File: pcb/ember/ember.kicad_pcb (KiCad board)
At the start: 2 copper layers, 139 x 108 mm, 101 parts, among them IC1 CD4051BM96, IC2 CD4051BM96, IC3 CD4051BM96, IC4 CD4051BM96, J2 USB_C_Receptacle_USB2.0, SW1 RESET, SW2 BOOT, U1 Hall_Sensor, U10 Hall_Sensor, U11 Hall_Sensor, U12 Hall_Sensor, U13 Hall_Sensor, U14 Hall_Sensor, U15 Hall_Sensor, U16 Hall_Sensor, U17 Hall_Sensor, U18 Hall_Sensor, U19 Hall_Sensor, U2 Hall_Sensor, U20 Hall_Sensor, U21 Hall_Sensor, U22 Hall_Sensor, U23 Hall_Sensor, U24 Hall_Sensor, U25 Hall_Sensor, U26 Hall_Sensor, U27 Hall_Sensor, U28 Hall_Sensor, U29 Hall_Sensor, U3 Hall_Sensor, U30 Hall_Sensor, U31 Hall_Sensor, U32 Hall_Sensor, U33 AMS1117-3.3, U4 Hall_Sensor, U5 Hall_Sensor, U6 Hall_Sensor, U7 Hall_Sensor, U8 Hall_Sensor, U9 Hall_Sensor, Y1 16MHz

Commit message: :wrench: ver1.1
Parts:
- removed D1: D_TVS_Dual_AAC, Package_TO_SOT_SMD:SOT-23
- removed TP1: SWCLK, TestPoint:TestPoint_THTPad_D1.0mm_Drill0.5mm
- removed TP2: GND, TestPoint:TestPoint_THTPad_D1.0mm_Drill0.5mm
- removed TP3: SWDIO, TestPoint:TestPoint_THTPad_D1.0mm_Drill0.5mm
- removed TP4: RESET, TestPoint:TestPoint_THTPad_D1.0mm_Drill0.5mm
- added J1: Conn_01x04_Socket, Connector_PinSocket_2.54mm:PinSocket_1x04_P2.54mm_Vertical, B.Cu at (154.0, 70.3)
- added U34: SRV05-4, Package_TO_SOT_SMD:SOT-23-6, B.Cu at (144.5, 33.0)
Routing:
- net GND: track 775.0 -> 892.8 mm, vias 128 -> 178
- net +3.3V: track 777.7 -> 810.3 mm
- net SWCLK: track 13.8 -> 27.9 mm
- net SWDIO: track 19.3 -> 29.7 mm
- net +5V: track 40.2 -> 47.2 mm, vias 3 -> 4
- net NRST: track 47.9 -> 41.4 mm, vias 2 -> 1
- net SENS_C_CH0: track 54.3 -> 60.6 mm
- net SENS_C_CH1: track 71.1 -> 76.7 mm
- net SENS_A_CH3: track 73.6 -> 79.1 mm
- net SENS_C_CH3: track 34.0 -> 39.0 mm
- net SENS_B_CH0: track 72.3 -> 77.3 mm
- net MUX_A: track 75.4 -> 78.0 mm
- net MUX_B: track 73.6 -> 75.9 mm
- net SENS_D_CH2: track 20.6 -> 22.8 mm
- net MUX_C: track 74.4 -> 76.2 mm
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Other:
- board text added: "Ember ver1.1 designed by @kenyoshizoe"
- board text added: "GND"
- board text added: "NRST"
- board text added: "SWCLK"
- board text added: "SWDIO"
- board text removed: "Ember ver1 designed by @kenyoshizoe"

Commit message: :sparkles: add eeprom
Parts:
- added IC5: M24C64-RMN6TP, ember:SOIC127P600X175-8N, B.Cu at (144.5, 56.2)
- added R6: 10k, Resistor_SMD:R_0603_1608Metric, B.Cu at (150.5, 60.8)
- added R7: 10k, Resistor_SMD:R_0603_1608Metric, B.Cu at (149.0, 60.8)
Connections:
- IC1 pad 10: MUX_B -> MUX2_B
- IC1 pad 11: MUX_A -> MUX2_A
- IC1 pad 3: ADC0 -> ADC3
- IC1 pad 9: MUX_C -> MUX2_C
- IC2 pad 10: MUX_B -> MUX2_B
- IC2 pad 11: MUX_A -> MUX2_A
- IC2 pad 3: ADC1 -> ADC4
- IC2 pad 9: MUX_C -> MUX2_C
- IC3 pad 10: MUX_B -> MUX1_B
- IC3 pad 11: MUX_A -> MUX1_A
- IC3 pad 9: MUX_C -> MUX1_C
- IC4 pad 10: MUX_B -> MUX1_B
- IC4 pad 11: MUX_A -> MUX1_A
- IC4 pad 3: ADC3 -> ADC1
- IC4 pad 9: MUX_C -> MUX1_C
- MCU1 pad 10: MUX_A -> MUX1_A
- MCU1 pad 11: MUX_B -> MUX1_B
- MCU1 pad 12: MUX_C -> MUX1_C
- MCU1 pad 13: ADC3 -> ADC1
- MCU1 pad 25: ADC1 -> ADC4
- MCU1 pad 26: ADC0 -> ADC3
- MCU1 pad 27: unconnected-(MCU1-PB14-Pad27) -> MUX2_C
- MCU1 pad 28: unconnected-(MCU1-PB15-Pad28) -> MUX2_B
- MCU1 pad 29: unconnected-(MCU1-PA8-Pad29) -> MUX2_A
- MCU1 pad 38: unconnected-(MCU1-PA15-Pad38) -> SCL
- MCU1 pad 42: unconnected-(MCU1-PB6-Pad42) -> WC
- MCU1 pad 43: unconnected-(MCU1-PB7-Pad43) -> SDA
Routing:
- net MUX_A: track 78.0 -> 0.00 mm, vias 4 -> 0
- net MUX_C: track 76.2 -> 0.00 mm, vias 4 -> 0
- net MUX_B: track 75.9 -> 0.00 mm, vias 4 -> 0
- net MUX1_A: track 0.00 -> 51.5 mm, vias 0 -> 3
- net MUX1_B: track 0.00 -> 51.4 mm, vias 0 -> 3
- net MUX1_C: track 0.00 -> 51.1 mm, vias 0 -> 3
- net ADC0: track 41.7 -> 0.00 mm, vias 2 -> 0
- net MUX2_A: track 0.00 -> 38.8 mm, vias 0 -> 3
- net MUX2_B: track 0.00 -> 37.1 mm, vias 0 -> 3
- net MUX2_C: track 0.00 -> 35.5 mm, vias 0 -> 3
- net SCL: track 0.00 -> 26.0 mm, vias 0 -> 2
- net GND: track 892.8 -> 917.1 mm, vias 178 -> 174
- net SDA: track 0.00 -> 23.4 mm, vias 0 -> 2
- net ADC1: track 19.6 -> 39.1 mm, vias 0 -> 2
- net ADC4: track 0.00 -> 19.6 mm
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
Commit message: :bug: add 1.5k pullup to D+
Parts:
- added R8: 1.5k, Resistor_SMD:R_0603_1608Metric, B.Cu at (138.0, 34.5)
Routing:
- net +3.3V: track 815.9 -> 820.0 mm
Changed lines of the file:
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@@
     )
   )
+  (footprint "Resistor_SMD:R_0603_1608Metric" (layer "B.Cu")
+    (at 138 34.5 -90)
+    (descr "Resistor SMD 0603 (1608 Metric), square (rectangular) end terminal, IPC_7351 nominal, (Body size source: IPC-SM-782 page 72, https://www.pcb-3d.com/wordpress/wp-content/uploads/ipc-sm-782a_amendment_1_and_2.pdf), generated with kicad-footprint-generator")
+    (tags "resistor")
+    (property "LCSC" "C22843")
+    (property "Sheetfile" "ember.kicad_sch")
+    (property "Sheetname" "")
+    (property "ki_description" "Resistor, small symbol")
+    (property "ki_keywords" "R resistor")
+    (attr smd)
+    (fp_text reference "R8" (at 0 1.43 90) (layer "B.SilkS")
+        (effects (font (size 1 1) (thickness 0.15)) (justify mirror))
+    )
+    (fp_text value "1.5k" (at 0 -1.43 90) (layer "B.Fab")
+        (effects (font (size 1 1) (thickness 0.15)) (justify mirror))
+    )
+    (fp_text user "${REFERENCE}" (at 0 0 90) (layer "B.Fab")
+        (effects (font (size 0.4 0.4) (thickness 0.06)) (justify mirror))
+    )
+    (fp_line (start -0.237258 -0.5225) (end 0.237258 -0.5225)
+      (stroke (width 0.12) (type solid)) (layer "B.SilkS"))
+    (fp_line (start -0.237258 0.5225) (end 0.237258 0.5225)
+      (stroke (width 0.12) (type solid)) (layer "B.SilkS"))
+    (fp_line (start -1.48 -0.73) (end -1.48 0.73)
+      (stroke (width 0.05) (type solid)) (layer "B.CrtYd"))
+    (fp_line (start -1.48 0.73) (end 1.48 0.73)
+      (stroke (width 0.05) (type solid)) (layer "B.CrtYd"))
+    (fp_line (start 1.48 -0.73) (end -1.48 -0.73)
+      (stroke (width 0.05) (type solid)) (layer "B.CrtYd"))
+    (fp_line (start 1.48 0.73) (end 1.48 -0.73)
+      (stroke (width 0.05) (type solid)) (layer "B.CrtYd"))
+    (fp_line (start -0.8 -0.4125) (end -0.8 0.4125)
+      (stroke (width 0.1) (type solid)) (layer "B.Fab"))
+    (fp_line (start -0.8 0.4125) (end 0.8 0.4125)
+      (stroke (width 0.1) (type solid)) (layer "B.Fab"))
+    (fp_line (start 0.8 -0.4125) (end -0.8 -0.4125)
+      (stroke (width 0.1) (type solid)) (layer "B.Fab"))
+    (fp_line (start 0.8 0.4125) (end 0.8 -0.4125)
+      (stroke (width 0.1) (type solid)) (layer "B.Fab"))
+    (pad "1" smd roundrect (at -0.825 0 270) (size 0.8 0.95) (layers "B.Cu" "B.Paste" "B.Mask") (roundrect_rratio 0.25)
+      (net 63 "USB_D+") (pintype "passive"))
+    (pad "2" smd roundrect (at 0.825 0 270) (size 0.8 0.95) (layers "B.Cu" "B.Paste" "B.Mask") (roundrect_rratio 0.25)
+      (net 14 "+3.3V") (pintype "passive"))
+    (model "${KICAD6_3DMODEL_DIR}/Resistor_SMD.3dshapes/R_0603_1608Metric.wrl"
+      (offset (xyz 0 0 0))
+      (scale (xyz 1 1 1))
+      (rotate (xyz 0 0 0))
+    )
+  )
   (footprint "Package_TO_SOT_SMD:SOT-23" (layer "B.Cu")
     (at 154 38 90)
@@
   (via (at 136 72) (size 0.8) (drill 0.4) (layers "F.Cu" "B.Cu") (net 14))
   (via (at 61.5 77) (size 0.8) (drill 0.4) (layers "F.Cu" "B.Cu") (net 14))
+  (segment (start 138 35.325) (end 138 38.75) (width 0.25) (layer "B.Cu") (net 14))
   (segment (start 124.1375 117.25) (end 103.1375 117.25) (width 0.25) (layer "B.Cu") (net 14))
   (segment (start 77.25 98.25) (end 58.6375 98.25) (width 0.25) (layer "B.Cu") (net 14))
@@
   (segment (start 82.75 89) (end 80.5 91.25) (width 0.25) (layer "B.Cu") (net 14))
   (segment (start 68.44375 116.94375) (end 69.45 115.9375) (width 0.25) (layer "B.Cu") (net 14))
+  (segment (start 138 38.75) (end 137.5 39.25) (width 0.25) (layer "B.Cu") (net 14))
   (segment (start 98.5625 54.9375) (end 97.95 54.9375) (width 0.25) (layer "B.Cu") (net 14))
   (segment (start 87.788 104.212) (end 74.75 117.25) (width 0.25) (layer "B.Cu") (net 14))
@@
   (via (at 127.025 54) (size 0.8) (drill 0.4) (layers "F.Cu" "B.Cu") (net 63))
   (via (at 127.871232 34.871232) (size 0.8) (drill 0.4) (layers "F.Cu" "B.Cu") (net 63))
-  (segment (start 129.093199 33.225) (end 140 33.225) (width 0.2) (layer "B.Cu") (net 63))
   (segment (start 127.871232 34.871232) (end 127.871232 34.446967) (width 0.2) (layer "B.Cu") (net 63))
   (segment (start 154.75 28.17) (end 154.75 28.995) (width 0.2) (layer "B.Cu") (net 63))
+  (segment (start 129.093199 33.225) (end 138 33.225) (width 0.2) (layer "B.Cu") (net 63))
   (segment (start 153.725 29.057501) (end 153.725 31.0932) (width 0.2) (layer "B.Cu") (net 63))
   (segment (start 145.0375 34.55) (end 141.325 34.55) (width 0.2) (layer "B.Cu") (net 63))
@@
   (segment (start 154.75 28.995) (end 154.7 29.045) (width 0.2) (layer "B.Cu") (net 63))
   (segment (start 153.75 29.032501) (end 153.725 29.057501) (width 0.2) (layer "B.Cu") (net 63))
+  (segment (start 138 33.675) (end 138 33.225) (width 0.2) (layer "B.Cu") (net 63))
   (segment (start 148.295313 33.225) (end 147.570313 33.95) (width 0.2) (layer "B.Cu") (net 63))
   (segment (start 126.725001 60.312501) (end 126.725001 54.299999) (width 0.2) (layer "B.Cu") (net 63))
+  (segment (start 138 33.225) (end 140 33.225) (width 0.2) (layer "B.Cu") (net 63))
   (segment (start 141.325 34.55) (end 140 33.225) (width 0.2) (layer "B.Cu") (net 63))
   (segment (start 126.75 60.3375) (end 126.725001 60.312501) (width 0.2) (layer "B.Cu") (net 63))

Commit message: :wrench: add VTref Pin
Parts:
- removed J1: Conn_01x04_Socket, Connector_PinSocket_2.54mm:PinSocket_1x04_P2.54mm_Vertical
- added J3: Conn_01x05_Socket, Connector_PinSocket_2.54mm:PinSocket_1x05_P2.54mm_Vertical, B.Cu at (163.5, 61.4)
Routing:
- net SWDIO: track 29.7 -> 38.5 mm
- net GND: track 917.1 -> 908.9 mm
- net SWCLK: track 27.9 -> 35.8 mm
- net +3.3V: track 820.0 -> 827.1 mm, vias 34 -> 35
- net NRST: track 41.4 -> 44.0 mm, vias 1 -> 0
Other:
- board text added: "VTref"

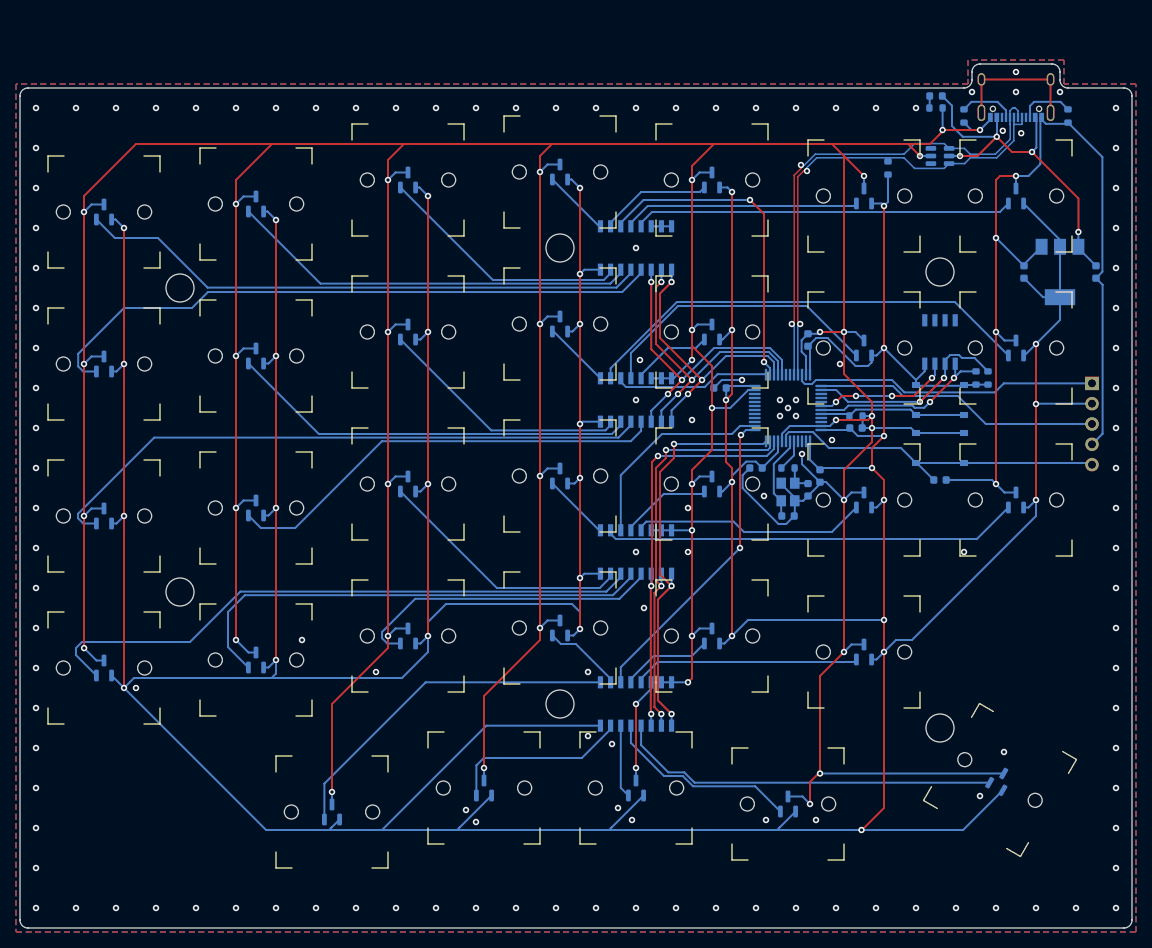
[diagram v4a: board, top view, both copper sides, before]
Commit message: change hall size 3.5mm→2.2mm(M2)
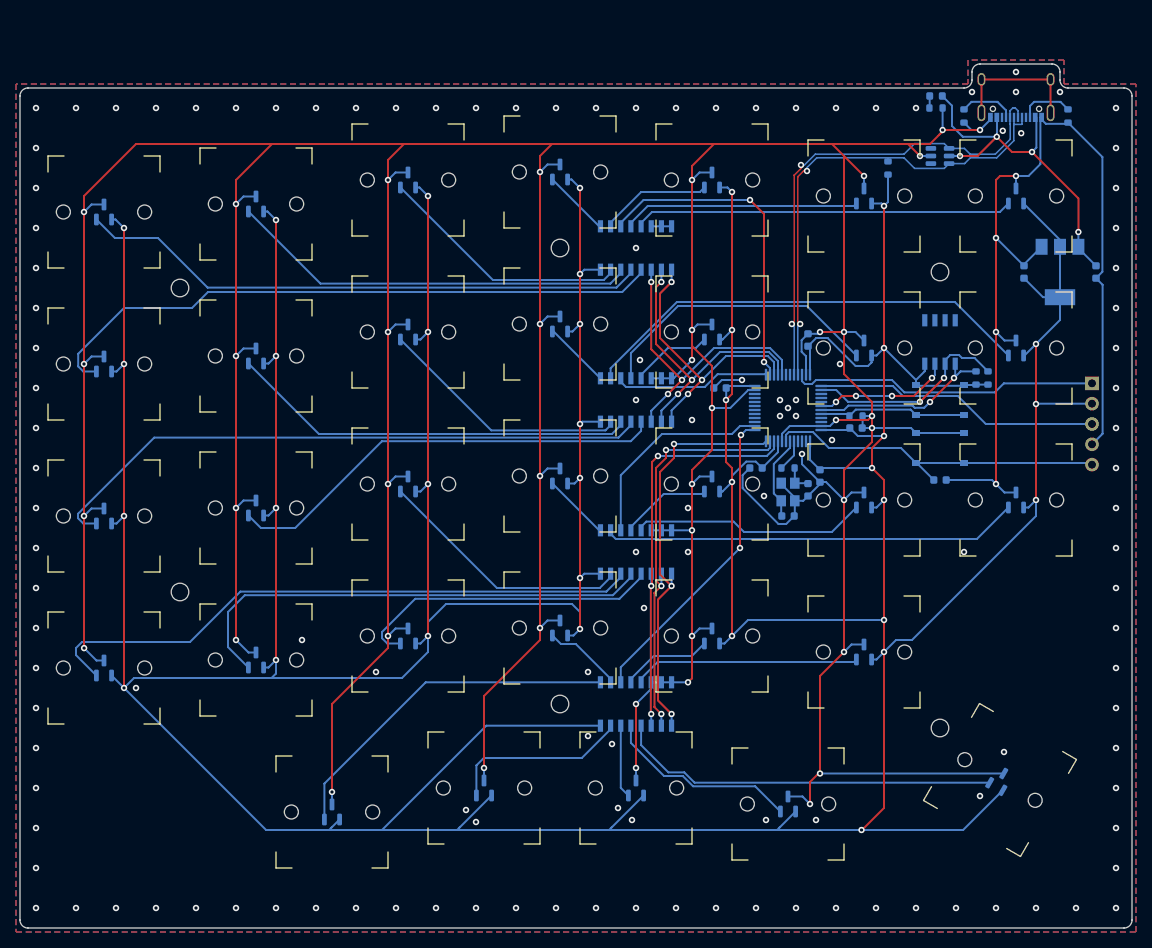
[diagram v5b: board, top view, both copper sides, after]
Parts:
- H33, H34, H35, H36, H37, H38: footprint MountingHole:MountingHole_3.5mm -> MountingHole:MountingHole_2.2mm_M2

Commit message: :sparkles: change usb connector position
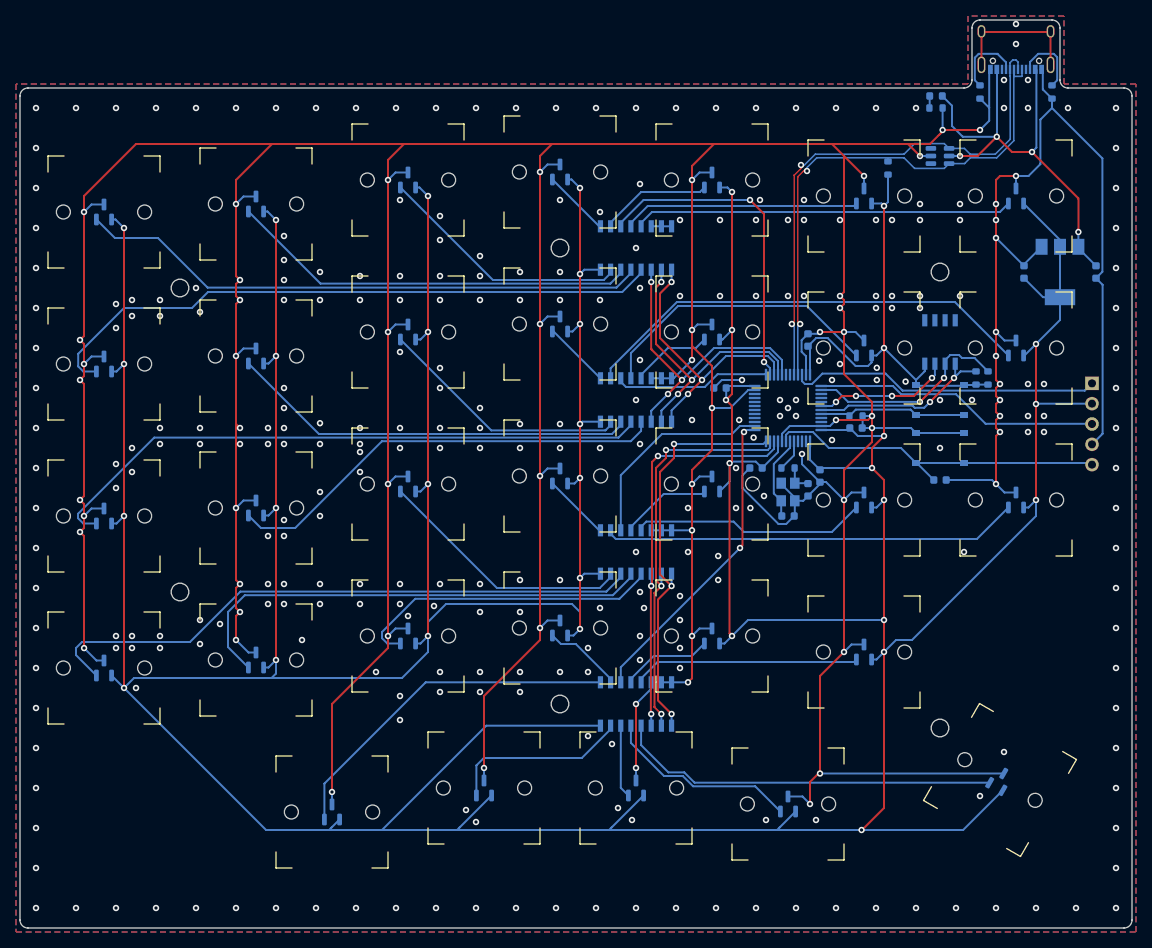
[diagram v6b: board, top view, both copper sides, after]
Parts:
- moved J2 6.00 mm to (154.0, 18.5)
- moved R1 3.61 mm to (149.5, 25.0)
- moved R2 3.61 mm to (158.5, 25.0)
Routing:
- net GND: track 908.9 -> 926.6 mm, vias 174 -> 362
- net +5V: track 47.2 -> 59.2 mm
- net USB_D+: track 60.4 -> 67.3 mm
- net USB_D-: track 61.1 -> 67.1 mm
- net Net-(J2-CC1): track 6.96 -> 9.14 mm
- net Net-(J2-CC2): track 6.78 -> 8.71 mm
- net +3.3V: track 827.1 -> 828.2 mm
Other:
- board size 139 x 108 mm -> 139 x 113.5 mm

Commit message: :sparkles: replace cd4052->ad708
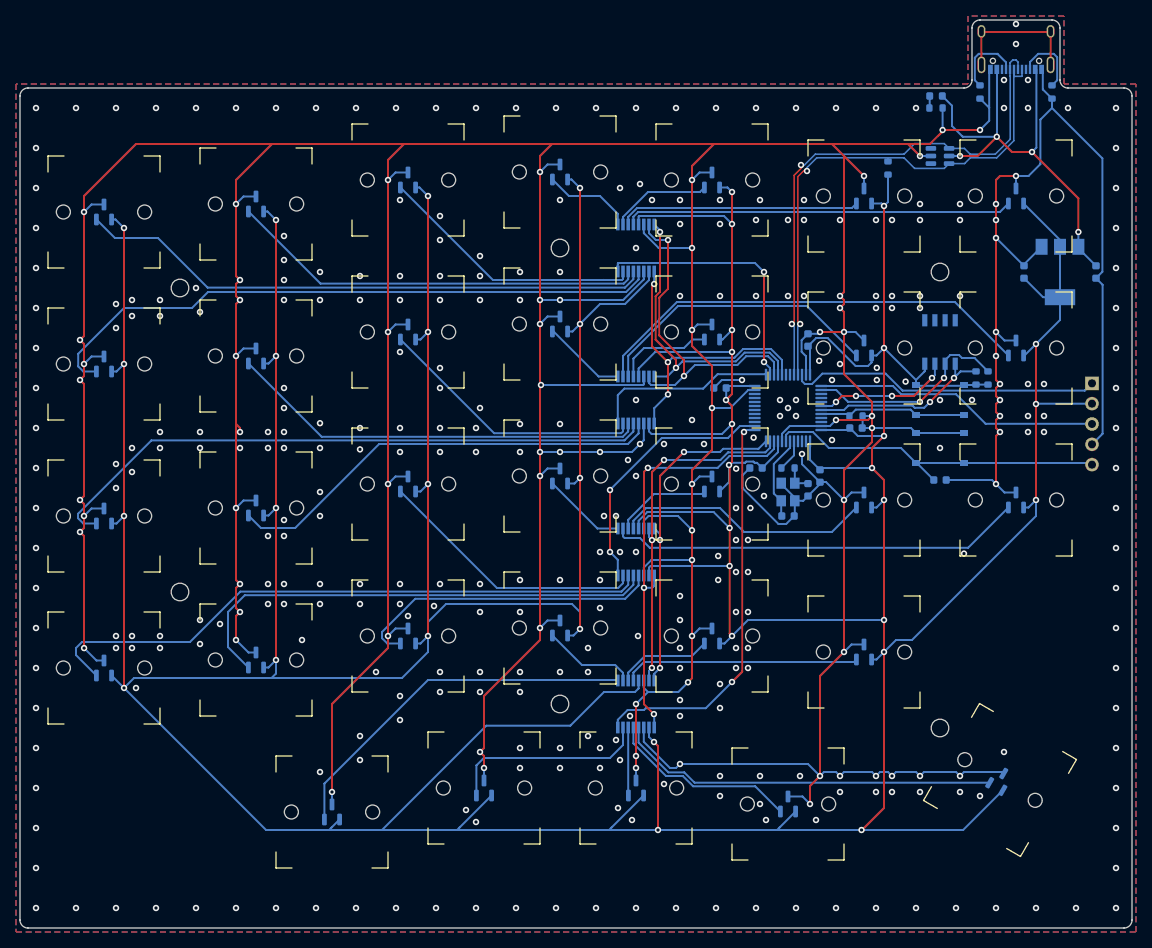
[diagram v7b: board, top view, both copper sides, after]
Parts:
- IC1, IC2, IC3, IC4: value CD4051BM96 -> ADG708BRUZ-REEL7; footprint ember:SOIC127P600X175-16N -> ember:SOP65P640X120-16N
- turned IC1 to 90 degrees
- turned IC2 to 90 degrees
- turned IC3 to 90 degrees
- turned IC4 to 90 degrees
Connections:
- IC1 pad 1: SENS_A_CH4 -> MUX2_A
- IC1 pad 10: MUX2_B -> SENS_A_CH6
- IC1 pad 11: MUX2_A -> SENS_A_CH7
- IC1 pad 12: SENS_A_CH3 -> SENS_A_CH5
- IC1 pad 13: SENS_A_CH0 -> +3.3V
- IC1 pad 14: SENS_A_CH1 -> GND
- IC1 pad 15: SENS_A_CH2 -> MUX2_C
- IC1 pad 16: +3.3V -> MUX2_B
- IC1 pad 2: SENS_A_CH6 -> +3.3V
- IC1 pad 3: ADC3 -> GND
- IC1 pad 4: SENS_A_CH7 -> SENS_A_CH3
- IC1 pad 5: SENS_A_CH5 -> SENS_A_CH0
- IC1 pad 6: GND -> SENS_A_CH1
- IC1 pad 7: GND -> SENS_A_CH2
- IC1 pad 8: GND -> ADC3
- IC1 pad 9: MUX2_C -> SENS_A_CH4
- IC2 pad 1: SENS_B_CH4 -> MUX2_A
- IC2 pad 10: MUX2_B -> SENS_B_CH6
- IC2 pad 11: MUX2_A -> SENS_B_CH7
- IC2 pad 12: SENS_B_CH3 -> SENS_B_CH5
- IC2 pad 13: SENS_B_CH0 -> +3.3V
- IC2 pad 14: SENS_B_CH1 -> GND
- IC2 pad 15: SENS_B_CH2 -> MUX2_C
- IC2 pad 16: +3.3V -> MUX2_B
- IC2 pad 2: SENS_B_CH6 -> +3.3V
- IC2 pad 3: ADC4 -> GND
- IC2 pad 4: SENS_B_CH7 -> SENS_B_CH3
- IC2 pad 5: SENS_B_CH5 -> SENS_B_CH0
- IC2 pad 6: GND -> SENS_B_CH1
- IC2 pad 7: GND -> SENS_B_CH2
- IC2 pad 8: GND -> ADC4
- IC2 pad 9: MUX2_C -> SENS_B_CH4
- IC3 pad 1: SENS_C_CH4 -> MUX1_A
- IC3 pad 10: MUX1_B -> SENS_C_CH6
- IC3 pad 11: MUX1_A -> SENS_C_CH7
- IC3 pad 12: SENS_C_CH3 -> SENS_C_CH5
- IC3 pad 13: SENS_C_CH0 -> +3.3V
- IC3 pad 14: SENS_C_CH1 -> GND
- IC3 pad 15: SENS_C_CH2 -> MUX1_B
- IC3 pad 16: +3.3V -> MUX1_C
- IC3 pad 2: SENS_C_CH6 -> +3.3V
- IC3 pad 3: ADC2 -> GND
- IC3 pad 4: SENS_C_CH7 -> SENS_C_CH3
- IC3 pad 5: SENS_C_CH5 -> SENS_C_CH0
- IC3 pad 6: GND -> SENS_C_CH1
- IC3 pad 7: GND -> SENS_C_CH2
- IC3 pad 8: GND -> ADC2
- IC3 pad 9: MUX1_C -> SENS_C_CH4
- IC4 pad 1: SENS_D_CH4 -> MUX1_A
- IC4 pad 10: MUX1_B -> SENS_D_CH6
- IC4 pad 11: MUX1_A -> SENS_D_CH7
- IC4 pad 12: SENS_D_CH3 -> SENS_D_CH5
- IC4 pad 13: SENS_D_CH0 -> +3.3V
- IC4 pad 14: SENS_D_CH1 -> GND
- IC4 pad 15: SENS_D_CH2 -> MUX1_B
- IC4 pad 16: +3.3V -> MUX1_C
- IC4 pad 2: SENS_D_CH6 -> +3.3V
- IC4 pad 3: ADC1 -> GND
- IC4 pad 4: SENS_D_CH7 -> SENS_D_CH3
- IC4 pad 5: SENS_D_CH5 -> SENS_D_CH0
- IC4 pad 6: GND -> SENS_D_CH1
- IC4 pad 7: GND -> SENS_D_CH2
- IC4 pad 8: GND -> ADC1
- IC4 pad 9: MUX1_C -> SENS_D_CH4
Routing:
- net +3.3V: track 828.2 -> 916.3 mm, vias 35 -> 39
- net GND: track 926.6 -> 1009.6 mm, vias 362 -> 411
- net ADC1: track 39.1 -> 50.5 mm
- net MUX1_C: track 51.1 -> 42.7 mm
- net ADC3: track 40.6 -> 32.9 mm
- net MUX2_C: track 35.5 -> 42.5 mm, vias 3 -> 2
- net MUX1_B: track 51.4 -> 44.6 mm
- net ADC2: track 26.2 -> 32.5 mm, vias 0 -> 2
- net ADC4: track 19.6 -> 23.2 mm
- net SENS_A_CH4: track 8.43 -> 11.3 mm
- net SENS_C_CH5: track 29.4 -> 32.0 mm
- net SENS_D_CH2: track 22.8 -> 25.3 mm
- net SENS_D_CH4: track 44.2 -> 46.6 mm
- net MUX1_A: track 51.5 -> 53.5 mm
- net SENS_B_CH4: track 8.43 -> 10.5 mm
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
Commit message: :sparkles: add 3d data
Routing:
- net GND: track 1009.6 -> 1015.0 mm, vias 411 -> 449
- net +3.3V: track 916.3 -> 917.2 mm
